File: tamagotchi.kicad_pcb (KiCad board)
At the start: 2 copper layers, 96 x 90.7 mm, 9 parts, among them SW1 SW_Push, SW2 SW_Push, SW3 SW_Push, U1 XIAO-ESP32-C3-SMD, U2 HS96L03W2C03, m3 MountingHole_3.2mm_M3

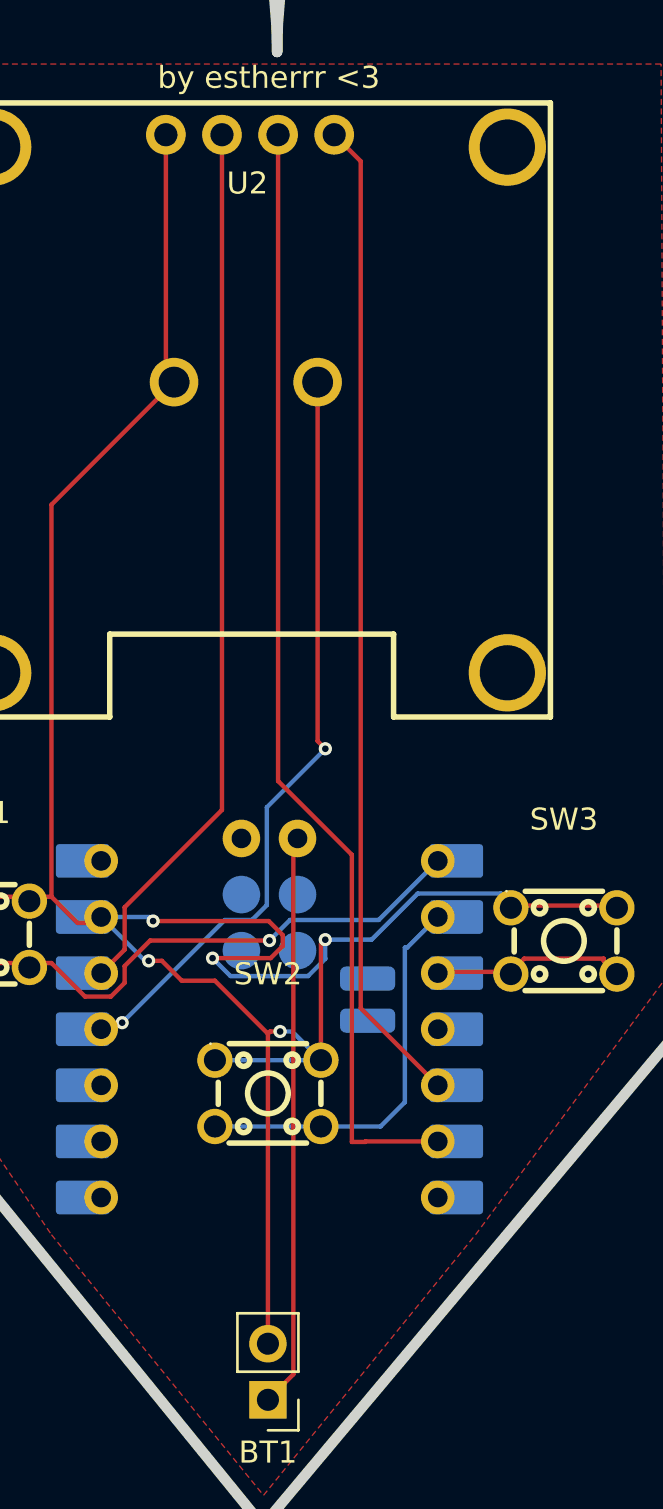
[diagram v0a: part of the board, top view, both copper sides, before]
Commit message: add new gerber files and changed the footprint mapping of the XIAO
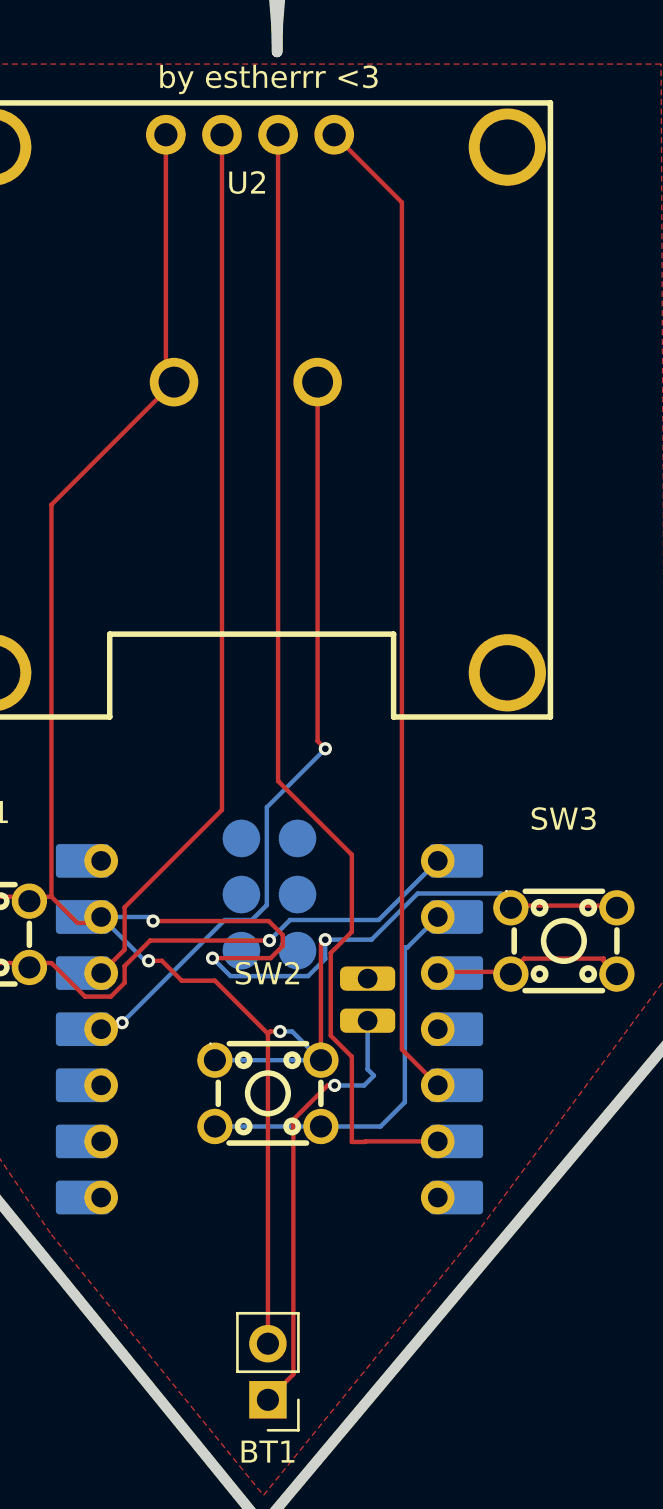
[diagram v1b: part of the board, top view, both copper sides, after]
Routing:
- net +BATT: track 26.1 -> 20.2 mm, vias 0 -> 1
- net Net-(U1-GPIO7_D5_SCL): track 50.9 -> 51.7 mm
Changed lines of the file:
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@@
 			(outputformat 1)
 			(mirror no)
-			(drillshape 1)
+			(drillshape 0)
 			(scaleselection 1)
-			(outputdirectory "")
+			(outputdirectory "gerbers/")
 		)
 	)
@@
 	(net 10 "unconnected-(U1-GPIO21_D6_TX-Pad7)")
 	(net 11 "unconnected-(U1-GPIO8_D8_SCK-Pad9)")
-	(net 12 "unconnected-(U1-GPIO9_D9_MISO-Pad10)")
-	(net 13 "+3V3")
-	(net 14 "unconnected-(U1-CHIP_EN-Pad19)")
-	(net 15 "+5V")
-	(net 16 "unconnected-(U1-GPIO9_D9_MISO-Pad10)_1")
-	(net 17 "Net-(U1-GPIO7_D5_SCL)")
-	(net 18 "unconnected-(U1-GPIO5_A3_D3-Pad4)")
-	(net 19 "unconnected-(U1-GND-Pad20)")
-	(net 20 "unconnected-(U1-GPIO5_A3_D3-Pad4)_1")
-	(net 21 "unconnected-(U1-MTMS-Pad21)")
-	(net 22 "unconnected-(U1-GPIO8_D8_SCK-Pad9)_1")
-	(net 23 "unconnected-(U1-MTDI-Pad17)")
-	(net 24 "unconnected-(U1-GPIO21_D6_TX-Pad7)_1")
-	(net 25 "unconnected-(U1-GND-Pad16)")
-	(net 26 "unconnected-(U1-GPIO20_D7_RX-Pad8)_1")
-	(net 27 "unconnected-(U1-MTDO-Pad18)")
+	(net 12 "+3V3")
+	(net 13 "unconnected-(U1-CHIP_EN-Pad19)")
+	(net 14 "+5V")
+	(net 15 "unconnected-(U1-GPIO9_D9_MISO-Pad10)_1")
+	(net 16 "Net-(U1-GPIO7_D5_SCL)")
+	(net 17 "unconnected-(U1-GPIO5_A3_D3-Pad4)")
+	(net 18 "unconnected-(U1-GND-Pad20)")
+	(net 19 "unconnected-(U1-MTMS-Pad21)")
+	(net 20 "unconnected-(U1-MTDI-Pad17)")
+	(net 21 "unconnected-(U1-GND-Pad16)")
+	(net 22 "unconnected-(U1-MTDO-Pad18)")
 	(footprint "easyeda2kicad:OLED-TH_L27.8-W27.2-P2.54_C9900033791"
 		(layer "F.Cu")
@@
 			(layers "*.Cu" "*.Mask")
 			(remove_unused_layers no)
-			(net 13 "+3V3")
+			(net 12 "+3V3")
 			(pinfunction "VCC")
 			(pintype "unspecified")
@@
 			(layers "*.Cu" "*.Mask")
 			(remove_unused_layers no)
-			(net 17 "Net-(U1-GPIO7_D5_SCL)")
+			(net 16 "Net-(U1-GPIO7_D5_SCL)")
 			(pinfunction "SCL")
 			(pintype "unspecified")
@@
 			(layers "*.Cu" "*.Mask")
 			(remove_unused_layers no)
-			(net 20 "unconnected-(U1-GPIO5_A3_D3-Pad4)_1")
+			(net 17 "unconnected-(U1-GPIO5_A3_D3-Pad4)")
 			(pinfunction "GPIO5_A3_D3")
 			(pintype "passive+no_connect")
@@
 			(layers "B.Cu" "B.Mask")
 			(roundrect_rratio 0.1)
-			(net 18 "unconnected-(U1-GPIO5_A3_D3-Pad4)")
+			(net 17 "unconnected-(U1-GPIO5_A3_D3-Pad4)")
 			(pinfunction "GPIO5_A3_D3")
 			(pintype "passive+no_connect")
@@
 			(layers "*.Cu" "*.Mask")
 			(remove_unused_layers no)
-			(net 17 "Net-(U1-GPIO7_D5_SCL)")
+			(net 16 "Net-(U1-GPIO7_D5_SCL)")
 			(pinfunction "GPIO7_D5_SCL")
 			(pintype "passive")
@@
 			(layers "B.Cu" "B.Mask")
 			(roundrect_rratio 0.1)
-			(net 17 "Net-(U1-GPIO7_D5_SCL)")
+			(net 16 "Net-(U1-GPIO7_D5_SCL)")
 			(pinfunction "GPIO7_D5_SCL")
 			(pintype "passive")
@@
 			(layers "*.Cu" "*.Mask")
 			(remove_unused_layers no)
-			(net 24 "unconnected-(U1-GPIO21_D6_TX-Pad7)_1")
+			(net 10 "unconnected-(U1-GPIO21_D6_TX-Pad7)")
 			(pinfunction "GPIO21_D6_TX")
 			(pintype "passive+no_connect")
@@
 			(layers "B.Cu" "B.Mask")
 			(roundrect_rratio 0.1)
-			(net 26 "unconnected-(U1-GPIO20_D7_RX-Pad8)_1")
+			(net 9 "unconnected-(U1-GPIO20_D7_RX-Pad8)")
 			(pinfunction "GPIO20_D7_RX")
 			(pintype "passive+no_connect")
@@
 			(layers "B.Cu" "B.Mask")
 			(roundrect_rratio 0.1)
-			(net 22 "unconnected-(U1-GPIO8_D8_SCK-Pad9)_1")
+			(net 11 "unconnected-(U1-GPIO8_D8_SCK-Pad9)")
 			(pinfunction "GPIO8_D8_SCK")
 			(pintype "passive+no_connect")
@@
 			(layers "B.Cu" "B.Mask")
 			(roundrect_rratio 0.1)
-			(net 12 "unconnected-(U1-GPIO9_D9_MISO-Pad10)")
+			(net 15 "unconnected-(U1-GPIO9_D9_MISO-Pad10)_1")
 			(pinfunction "GPIO9_D9_MISO")
 			(pintype "passive+no_connect")
@@
 			(layers "*.Cu" "*.Mask")
 			(remove_unused_layers no)
-			(net 16 "unconnected-(U1-GPIO9_D9_MISO-Pad10)_1")
+			(net 15 "unconnected-(U1-GPIO9_D9_MISO-Pad10)_1")
 			(pinfunction "GPIO9_D9_MISO")
 			(pintype "passive+no_connect")
@@
 			(layers "B.Cu" "B.Mask")
 			(roundrect_rratio 0.1)
-			(net 13 "+3V3")
+			(net 12 "+3V3")
 			(pinfunction "3V3")
 			(pintype "passive")
@@
 			(layers "*.Cu" "*.Mask")
 			(remove_unused_layers no)
-			(net 13 "+3V3")
+			(net 12 "+3V3")
 			(pinfunction "3V3")
 			(pintype "passive")
@@
 			(layers "B.Cu" "B.Mask")
 			(roundrect_rratio 0.1)
-			(net 15 "+5V")
+			(net 14 "+5V")
 			(pinfunction "5V")
 			(pintype "passive")
@@
 			(layers "*.Cu" "*.Mask")
 			(remove_unused_layers no)
-			(net 15 "+5V")
+			(net 14 "+5V")
 			(pinfunction "5V")
 			(pintype "passive")
 		)
-		(pad "15" thru_hole circle
-			(at 8.636 1.27)
-			(size 1.7 1.7)
+		(pad "15" thru_hole roundrect
+			(at 0.386 4.445)
+			(size 2.5 1.1)
 			(drill 0.889)
 			(layers "*.Cu" "*.Mask")
 			(remove_unused_layers no)
+			(roundrect_rratio 0.25)
 			(net 2 "+BATT")
 			(pinfunction "BAT")
 			(pintype "passive")
+			(thermal_bridge_angle 45)
 		)
-		(pad "16" thru_hole circle
-			(at 8.636 -1.27)
-			(size 1.7 1.7)
+		(pad "16" thru_hole roundrect
+			(at 2.291 4.445)
+			(size 2.5 1.1)
 			(drill 0.889)
 			(layers "*.Cu" "*.Mask")
 			(remove_unused_layers no)
-			(net 25 "unconnected-(U1-GND-Pad16)")
+			(roundrect_rratio 0.25)
+			(net 21 "unconnected-(U1-GND-Pad16)")
 			(pinfunction "GND")
 			(pintype "passive")
+			(thermal_bridge_angle 45)
 		)
 		(pad "17" smd circle
-			(at 6.096 1.27 180)
+			(at 8.636 1.27 180)
 			(size 1.7 1.7)
 			(layers "B.Cu" "B.Mask" "B.Paste")
-			(net 23 "unconnected-(U1-MTDI-Pad17)")
+			(net 20 "unconnected-(U1-MTDI-Pad17)")
 			(pinfunction "MTDI")
 			(pintype "passive+no_connect")
 		)
 		(pad "18" smd circle
-			(at 6.096 -1.27 180)
+			(at 8.636 -1.27 180)
 			(size 1.7 1.7)
 			(layers "B.Cu" "B.Mask" "B.Paste")
-			(net 27 "unconnected-(U1-MTDO-Pad18)")
+			(net 22 "unconnected-(U1-MTDO-Pad18)")
 			(pinfunction "MTDO")
 			(pintype "passive+no_connect")
 		)
 		(pad "19" smd circle
-			(at 3.556 1.27 180)
+			(at 6.096 1.27 180)
 			(size 1.7 1.7)
 			(layers "B.Cu" "B.Mask" "B.Paste")
-			(net 14 "unconnected-(U1-CHIP_EN-Pad19)")
+			(net 13 "unconnected-(U1-CHIP_EN-Pad19)")
 			(pinfunction "CHIP_EN")
 			(pintype "passive+no_connect")
 		)
 		(pad "20" smd circle
-			(at 3.556 -1.27 180)
+			(at 6.096 -1.27 180)
 			(size 1.7 1.7)
 			(layers "B.Cu" "B.Mask" "B.Paste")
-			(net 19 "unconnected-(U1-GND-Pad20)")
+			(net 18 "unconnected-(U1-GND-Pad20)")
 			(pinfunction "GND")
 			(pintype "passive+no_connect")
 		)
-		(pad "21" smd roundrect
-			(at 0.386 4.445)
-			(size 2.5 1.1)
+		(pad "21" smd circle
+			(at 3.556 1.27 180)
+			(size 1.7 1.7)
 			(layers "B.Cu" "B.Mask" "B.Paste")
-			(roundrect_rratio 0.25)
-			(net 21 "unconnected-(U1-MTMS-Pad21)")
+			(net 19 "unconnected-(U1-MTMS-Pad21)")
 			(pinfunction "MTMS")
 			(pintype "passive+no_connect")
-			(thermal_bridge_angle 45)
 		)
-		(pad "22" smd roundrect
-			(at 2.291 4.445)
-			(size 2.5 1.1)
+		(pad "22" smd circle
+			(at 3.556 -1.27 180)
+			(size 1.7 1.7)
 			(layers "B.Cu" "B.Mask" "B.Paste")
-			(roundrect_rratio 0.25)
 			(net 7 "unconnected-(U1-MTCK-Pad22)")
 			(pinfunction "MTCK")
 			(pintype "passive+no_connect")
-			(thermal_bridge_angle 45)
 		)
 		(embedded_fonts no)
@@
 	)
 	(segment
-		(start 74.6 85)
-		(end 74.351 85.249)
+		(start 74.351 109.324)
+		(end 74.351 97.79195)
+		(width 0.2)
+		(layer "F.Cu")
+		(net 2)
+	)
+	(segment
+		(start 74.351 97.79195)
+		(end 75.901684 96.241266)
 		(width 0.2)
 		(layer "F.Cu")
@@
 	)
 	(segment
-		(start 74.351 85.249)
-		(end 74.351 109.324)
+		(start 75.901684 96.241266)
+		(end 76.222509 96.241266)
 		(width 0.2)
 		(layer "F.Cu")
@@
 		(net 2)
 	)
+	(via
+		(at 76.222509 96.241266)
+		(size 0.6)
+		(drill 0.3)
+		(layers "F.Cu" "B.Cu")
+		(net 2)
+	)
+	(segment
+		(start 77.715 95.515)
+		(end 77.715 93.31)
+		(width 0.2)
+		(layer "B.Cu")
+		(net 2)
+	)
+	(segment
+		(start 78 95.8)
+		(end 77.715 95.515)
+		(width 0.2)
+		(layer "B.Cu")
+		(net 2)
+	)
+	(segment
+		(start 77.558734 96.241266)
+		(end 78 95.8)
+		(width 0.2)
+		(layer "B.Cu")
+		(net 2)
+	)
+	(segment
+		(start 76.222509 96.241266)
+		(end 77.558734 96.241266)
+		(width 0.2)
+		(layer "B.Cu")
+		(net 2)
+	)
 	(segment
 		(start 75.45 80.65)
@@
 	)
 	(segment
-		(start 76.2 53.2)
-		(end 77.401 54.401)
+		(start 80.89 96.236)
+		(end 79.266 94.612)
 		(width 0.2)
 		(layer "F.Cu")
@@
 	)
 	(segment
-		(start 77.401 54.401)
-		(end 77.401 92.747)
+		(start 79.266 56.266)
+		(end 76.2 53.2)
 		(width 0.2)
 		(layer "F.Cu")
@@
 	)
 	(segment
-		(start 77.401 92.747)
-		(end 80.89 96.236)
+		(start 79.266 94.612)
+		(end 79.266 56.266)
 		(width 0.2)
 		(layer "F.Cu")
@@
 		(width 0.2)
 		(layer "F.Cu")
-		(net 13)
+		(net 12)
 	)
 	(segment
@@
 		(width 0.2)
 		(layer "F.Cu")
-		(net 13)
+		(net 12)
 	)
 	(segment
@@
 		(width 0.2)
 		(layer "F.Cu")
-		(net 13)
+		(net 12)
 	)
 	(segment
@@
 		(width 0.2)
 		(layer "F.Cu")
-		(net 13)
+		(net 12)
 	)
 	(segment
-		(start 77 85.8)
-		(end 77 98.8)
+		(start 76.044392 93.987342)
+		(end 76.044392 90.24466)
 		(width 0.2)
 		(layer "F.Cu")
-		(net 17)
+		(net 16)
 	)
 	(segment
@@
 		(width 0.2)
 		(layer "F.Cu")
-		(net 17)
+		(net 16)
 	)
 	(segment
@@
 		(width 0.2)
 		(layer "F.Cu")
-		(net 17)
+		(net 16)
+	)
+	(segment
+		(start 77 94.94295)
+		(end 76.044392 93.987342)
+		(width 0.2)
+		(layer "F.Cu")
+		(net 16)
 	)
 	(segment
@@
 		(width 0.2)
 		(layer "F.Cu")
-		(net 17)
+		(net 16)
+	)
+	(segment
+		(start 77 89.289052)
+		(end 77 85.8)
+		(width 0.2)
+		(layer "F.Cu")
+		(net 16)
 	)
 	(segment
@@
 		(width 0.2)
 		(layer "F.Cu")
-		(net 17)
+		(net 16)
+	)
+	(segment
+		(start 76.044392 90.24466)
+		(end 77 89.289052)
+		(width 0.2)
+		(layer "F.Cu")
+		(net 16)
+	)
+	(segment
+		(start 77 98.8)
+		(end 77 94.94295)
+		(width 0.2)
+		(layer "F.Cu")
+		(net 16)
 	)
 	(segment
@@
 		(width 0.2)
 		(layer "F.Cu")
-		(net 17)
+		(net 16)
 	)
 	(zone
